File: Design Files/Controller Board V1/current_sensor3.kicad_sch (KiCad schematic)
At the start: 5 parts, among them U4 INA219BIDR

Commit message: resistor footprints
yuh
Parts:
- R1: renamed from R4; footprint (none) -> Resistor_SMD:R_0805_2012Metric
- R2: renamed from R9; footprint (none) -> Resistor_SMD:R_0603_1608Metric
- R3: renamed from R10; footprint (none) -> Resistor_SMD:R_0603_1608Metric
- R4: renamed from R11; footprint (none) -> Resistor_SMD:R_0603_1608Metric
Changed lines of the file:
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@@
 		(on_board yes)
 		(dnp no)
-		(property "Reference" "R11"
+		(property "Reference" "R4"
 			(at 170.18 87.884 0)
 			(effects
@@
 			)
 		)
-		(property "Footprint" ""
+		(property "Footprint" "Resistor_SMD:R_0603_1608Metric"
 			(at 169.672 88.9 90)
 			(effects
@@
 			(project "Control Board V1"
 				(path "/e0c606b8-cbb9-4aff-b96c-73876da6ca74/f9ccd444-bb08-4521-9886-c035e86d8847"
-					(reference "R11")
+					(reference "R4")
 					(unit 1)
 				)
@@
 		(on_board yes)
 		(dnp no)
-		(property "Reference" "R10"
+		(property "Reference" "R3"
 			(at 163.83 87.884 0)
 			(effects
@@
 			)
 		)
-		(property "Footprint" ""
+		(property "Footprint" "Resistor_SMD:R_0603_1608Metric"
 			(at 163.322 88.9 90)
 			(effects
@@
 			(project "Control Board V1"
 				(path "/e0c606b8-cbb9-4aff-b96c-73876da6ca74/f9ccd444-bb08-4521-9886-c035e86d8847"
-					(reference "R10")
+					(reference "R3")
 					(unit 1)
 				)
@@
 		(on_board yes)
 		(dnp no)
-		(property "Reference" "R9"
+		(property "Reference" "R2"
 			(at 157.48 87.884 0)
 			(effects
@@
 			)
 		)
-		(property "Footprint" ""
+		(property "Footprint" "Resistor_SMD:R_0603_1608Metric"
 			(at 156.972 88.9 90)
 			(effects
@@
 			(project "Control Board V1"
 				(path "/e0c606b8-cbb9-4aff-b96c-73876da6ca74/f9ccd444-bb08-4521-9886-c035e86d8847"
-					(reference "R9")
+					(reference "R2")
 					(unit 1)
 				)
@@
 		(dnp no)
 		(fields_autoplaced yes)
-		(property "Reference" "R4"
+		(property "Reference" "R1"
 			(at 139.7 76.2 90)
 			(effects
@@
 			)
 		)
-		(property "Footprint" ""
+		(property "Footprint" "Resistor_SMD:R_0805_2012Metric"
 			(at 139.7 84.328 90)
 			(effects
@@
 			(project "Control Board V1"
 				(path "/e0c606b8-cbb9-4aff-b96c-73876da6ca74/f9ccd444-bb08-4521-9886-c035e86d8847"
-					(reference "R4")
-					(unit 1)
-				)
+					(reference "R1")
+					(unit 1)
+				)

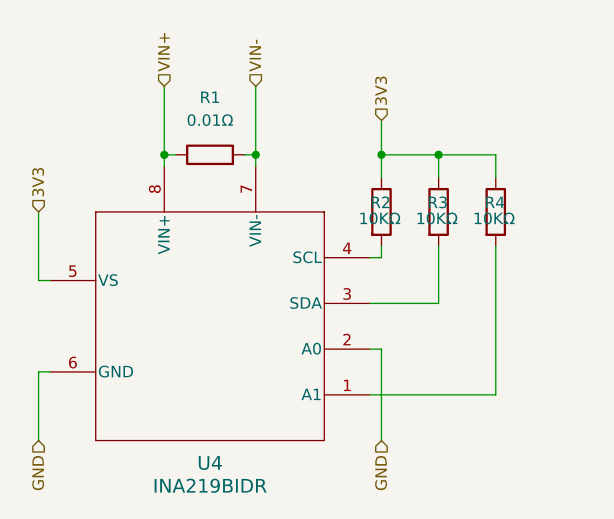
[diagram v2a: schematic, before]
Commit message: I2C channels for pico and current sensors
gaming B)
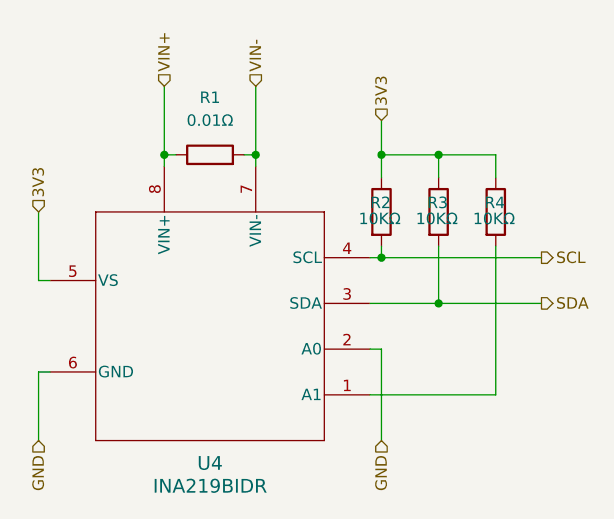
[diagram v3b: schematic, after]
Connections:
- net SDA: now reaches R3.2, U4.3 (SDA)
- net SCL: now reaches R2.2, U4.4 (SCL)
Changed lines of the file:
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@@
 	(paper "A4")
 	(junction
+		(at 165.1 99.06)
+		(diameter 0)
+		(color 0 0 0 0)
+	)
+	(junction
 		(at 134.62 82.55)
 		(diameter 0)
@@
 	)
 	(junction
+		(at 158.75 93.98)
+		(diameter 0)
+		(color 0 0 0 0)
+	)
+	(junction
 		(at 144.78 82.55)
 		(diameter 0)
@@
 	(wire
 		(pts
+			(xy 158.75 93.98) (xy 176.53 93.98)
+		)
+		(stroke
+			(width 0)
+			(type default)
+		)
+	)
+	(wire
+		(pts
 			(xy 144.78 74.93) (xy 144.78 82.55)
 		)
@@
 	(wire
 		(pts
+			(xy 165.1 99.06) (xy 176.53 99.06)
+		)
+		(stroke
+			(width 0)
+			(type default)
+		)
+	)
+	(wire
+		(pts
 			(xy 158.75 85.09) (xy 158.75 82.55)
 		)
@@
 		(shape input)
 		(at 120.65 88.9 90)
+		(fields_autoplaced yes)
+		(effects
+			(font
+				(size 1.27 1.27)
+			)
+			(justify left)
+		)
+	)
+	(hierarchical_label "SDA"
+		(shape output)
+		(at 176.53 99.06 0)
+		(fields_autoplaced yes)
 		(effects
 			(font
@@
 		(shape input)
 		(at 158.75 114.3 270)
+		(fields_autoplaced yes)
 		(effects
 			(font
@@
 		(shape input)
 		(at 158.75 78.74 90)
+		(fields_autoplaced yes)
 		(effects
 			(font
@@
 		(shape input)
 		(at 134.62 74.93 90)
+		(fields_autoplaced yes)
 		(effects
 			(font
@@
 		(shape input)
 		(at 120.65 114.3 270)
+		(fields_autoplaced yes)
 		(effects
 			(font
@@
 		)
 	)
+	(hierarchical_label "SCL"
+		(shape output)
+		(at 176.53 93.98 0)
+		(fields_autoplaced yes)
+		(effects
+			(font
+				(size 1.27 1.27)
+			)
+			(justify left)
+		)
+	)
 	(hierarchical_label "VIN-"
 		(shape input)
 		(at 144.78 74.93 90)
-		(effects
-			(font
+		(fields_autoplaced yes)
+		(effects
+			(font

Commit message: Assigning footprints and ading to schematic
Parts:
- renumbered R2 to R10, R3 to R11, R4 to R12, R1 to R9
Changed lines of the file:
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@@
 		(shape input)
 		(at 120.65 88.9 90)
-		(fields_autoplaced yes)
 		(effects
 			(font
@@
 		(shape output)
 		(at 176.53 99.06 0)
-		(fields_autoplaced yes)
 		(effects
 			(font
@@
 		(shape input)
 		(at 158.75 114.3 270)
-		(fields_autoplaced yes)
 		(effects
 			(font
@@
 		(shape input)
 		(at 158.75 78.74 90)
-		(fields_autoplaced yes)
 		(effects
 			(font
@@
 		(shape input)
 		(at 134.62 74.93 90)
-		(fields_autoplaced yes)
 		(effects
 			(font
@@
 		(shape input)
 		(at 120.65 114.3 270)
-		(fields_autoplaced yes)
 		(effects
 			(font
@@
 		(shape output)
 		(at 176.53 93.98 0)
-		(fields_autoplaced yes)
 		(effects
 			(font
@@
 		(shape input)
 		(at 144.78 74.93 90)
-		(fields_autoplaced yes)
 		(effects
 			(font
@@
 		(on_board yes)
 		(dnp no)
-		(property "Reference" "R4"
+		(property "Reference" "R12"
 			(at 170.18 87.884 0)
 			(effects
@@
 			(project "Control Board V1"
 				(path "/e0c606b8-cbb9-4aff-b96c-73876da6ca74/f9ccd444-bb08-4521-9886-c035e86d8847"
-					(reference "R4")
+					(reference "R12")
 					(unit 1)
 				)
@@
 		(on_board yes)
 		(dnp no)
-		(property "Reference" "R3"
+		(property "Reference" "R11"
 			(at 163.83 87.884 0)
 			(effects
@@
 			(project "Control Board V1"
 				(path "/e0c606b8-cbb9-4aff-b96c-73876da6ca74/f9ccd444-bb08-4521-9886-c035e86d8847"
-					(reference "R3")
+					(reference "R11")
 					(unit 1)
 				)
@@
 		(on_board yes)
 		(dnp no)
-		(property "Reference" "R2"
+		(property "Reference" "R10"
 			(at 157.48 87.884 0)
 			(effects
@@
 			(project "Control Board V1"
 				(path "/e0c606b8-cbb9-4aff-b96c-73876da6ca74/f9ccd444-bb08-4521-9886-c035e86d8847"
-					(reference "R2")
+					(reference "R10")
 					(unit 1)
 				)
@@
 		(dnp no)
 		(fields_autoplaced yes)
-		(property "Reference" "R1"
+		(property "Reference" "R9"
 			(at 139.7 76.2 90)
 			(effects
@@
 			(project "Control Board V1"
 				(path "/e0c606b8-cbb9-4aff-b96c-73876da6ca74/f9ccd444-bb08-4521-9886-c035e86d8847"
-					(reference "R1")
+					(reference "R9")
 					(unit 1)
 				)

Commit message: here we go agane
Updating footprints and tackling general layout
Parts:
- added C6: 100 nF, Capacitor_SMD:C_0603_1608Metric, symbol Device:C
- U4: footprint D0008A_N -> Library:INA219
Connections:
- net 3V3: now also C6.1
- net GND: now also C6.2
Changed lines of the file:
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@@
+	)
+	(junction
+		(at 120.65 106.68)
+		(diameter 0)
+		(color 0 0 0 0)
 	)
 	(junction
@@
 	)
 	(junction
+		(at 120.65 96.52)
+		(diameter 0)
+		(color 0 0 0 0)
+	)
+	(junction
 		(at 158.75 82.55)
 		(diameter 0)
@@
 	(wire
 		(pts
+			(xy 120.65 96.52) (xy 120.65 97.79)
+		)
+		(stroke
+			(width 0)
+			(type default)
+		)
+	)
+	(wire
+		(pts
 			(xy 157.48 104.14) (xy 158.75 104.14)
 		)
@@
 		(pts
 			(xy 120.65 106.68) (xy 120.65 114.3)
+		)
+		(stroke
+			(width 0)
+			(type default)
+		)
+	)
+	(wire
+		(pts
+			(xy 120.65 105.41) (xy 120.65 106.68)
 		)
 		(stroke
@@
 	)
 	(symbol
+		(lib_id "Device:C")
+		(at 120.65 101.6 0)
+		(unit 1)
+		(exclude_from_sim no)
+		(in_bom yes)
+		(on_board yes)
+		(dnp no)
+		(fields_autoplaced yes)
+		(property "Reference" "C6"
+			(at 124.46 100.3299 0)
+			(effects
+				(font
+					(size 1.27 1.27)
+				)
+				(justify left)
+			)
+		)
+		(property "Value" "100 nF"
+			(at 124.46 102.8699 0)
+			(effects
+				(font
+					(size 1.27 1.27)
+				)
+				(justify left)
+			)
+		)
+		(property "Footprint" "Capacitor_SMD:C_0603_1608Metric"
+			(at 121.6152 105.41 0)
+			(effects
+				(font
+					(size 1.27 1.27)
+				)
+				(hide yes)
+			)
+		)
+		(property "Datasheet" "~"
+			(at 120.65 101.6 0)
+			(effects
+				(font
+					(size 1.27 1.27)
+				)
+				(hide yes)
+			)
+		)
+		(property "Description" "Unpolarized capacitor"
+			(at 120.65 101.6 0)
+			(effects
+				(font
+					(size 1.27 1.27)
+				)
+				(hide yes)
+			)
+		)
+		(property "MANUFACTURER" ""
+			(at 120.65 101.6 0)
+			(effects
+				(font
+					(size 1.27 1.27)
+				)
+				(hide yes)
+			)
+		)
+		(property "MAXIMUM_PACKAGE_HEIGHT" ""
+			(at 120.65 101.6 0)
+			(effects
+				(font
+					(size 1.27 1.27)
+				)
+				(hide yes)
+			)
+		)
+		(property "PARTREV" ""
+			(at 120.65 101.6 0)
+			(effects
+				(font
+					(size 1.27 1.27)
+				)
+				(hide yes)
+			)
+		)
+		(property "SNAPEDA_PN" ""
+			(at 120.65 101.6 0)
+			(effects
+				(font
+					(size 1.27 1.27)
+				)
+				(hide yes)
+			)
+		)
+		(property "STANDARD" ""
+			(at 120.65 101.6 0)
+			(effects
+				(font
+					(size 1.27 1.27)
+				)
+				(hide yes)
+			)
+		)
+		(pin "1"
+		)
+		(pin "2"
+		)
+		(instances
+			(project "Control Board V1"
+				(path "/e0c606b8-cbb9-4aff-b96c-73876da6ca74/f9ccd444-bb08-4521-9886-c035e86d8847"
+					(reference "C6")
+					(unit 1)
+				)
+			)
+		)
+	)
+	(symbol
 		(lib_id "Device:R")
 		(at 158.75 88.9 0)
@@
 			)
 		)
-		(property "Footprint" "D0008A_N"
+		(property "Footprint" "Library:INA219"
 			(at 139.7 101.6 0)
 			(effects
